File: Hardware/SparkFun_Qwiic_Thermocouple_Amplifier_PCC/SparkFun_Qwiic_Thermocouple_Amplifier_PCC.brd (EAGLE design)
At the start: 22.9 x 39.4 mm, 49 parts, among them J1 PTH, U16 MCP9600-SMD

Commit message: Added screw terminal board
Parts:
- removed I2C: (no value), SparkFun-Jumpers:SMT-JUMPER_3_2-NC_TRACE_SILK
- removed U16: MCP9600-SMD, MCP9600:MQFN-20
- added J5: PCB_THERMOCOUPLE, SparkFun-Electromechanical:PCC-SMP
- added U$15: (no value), buzzard_labels (7):ADR_#_0X660
- added U1: MCP9600-SMD, SparkFun-IC-Conversion:MQFN-20
- J1: device SparkX:1X04_NO_SILK -> SparkFun-Connectors:1X04_NO_SILK
- J2, J3: value (none) -> QWIIC
- JP2: value PCB_THERMOCOUPLE -> I2C; device MCP9600:PCC-SMP -> SparkFun-Jumpers:SMT-JUMPER_3_2-NC_TRACE_SILK
- moved JP2 8.71 mm to (15.9, 16.6), flipped to the top
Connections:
- net !ALT1: now also U1.11; no longer U16.11
- net !ALT2: now also U1.12; no longer U16.12
- net !ALT3: now also U1.14; no longer U16.14
- net !ALT4: now also U1.15; no longer U16.15
- net 3.3V: now also JP2.2, U1.8; no longer I2C.2, U16.8
- net ADDR: now also U1.16; no longer U16.16
- net GND: now also U1.1, U1.10, U1.13, U1.17, U1.18, U1.21, U1.3, U1.5, U1.6, U1.7, U1.9; no longer U16.1, U16.10, U16.13, U16.17, U16.18, U16.21, U16.3, U16.5, U16.6, U16.7, U16.9
- net N$2: now also JP2.1; no longer I2C.1
- net N$3: now also JP2.3; no longer I2C.3
- net N$4: now also J5.+, U1.2; no longer JP2.+, U16.2
- net N$5: now also J5.-, U1.4; no longer JP2.-, U16.4
- net SCL: now also U1.19; no longer U16.19
- net SDA: now also U1.20; no longer U16.20

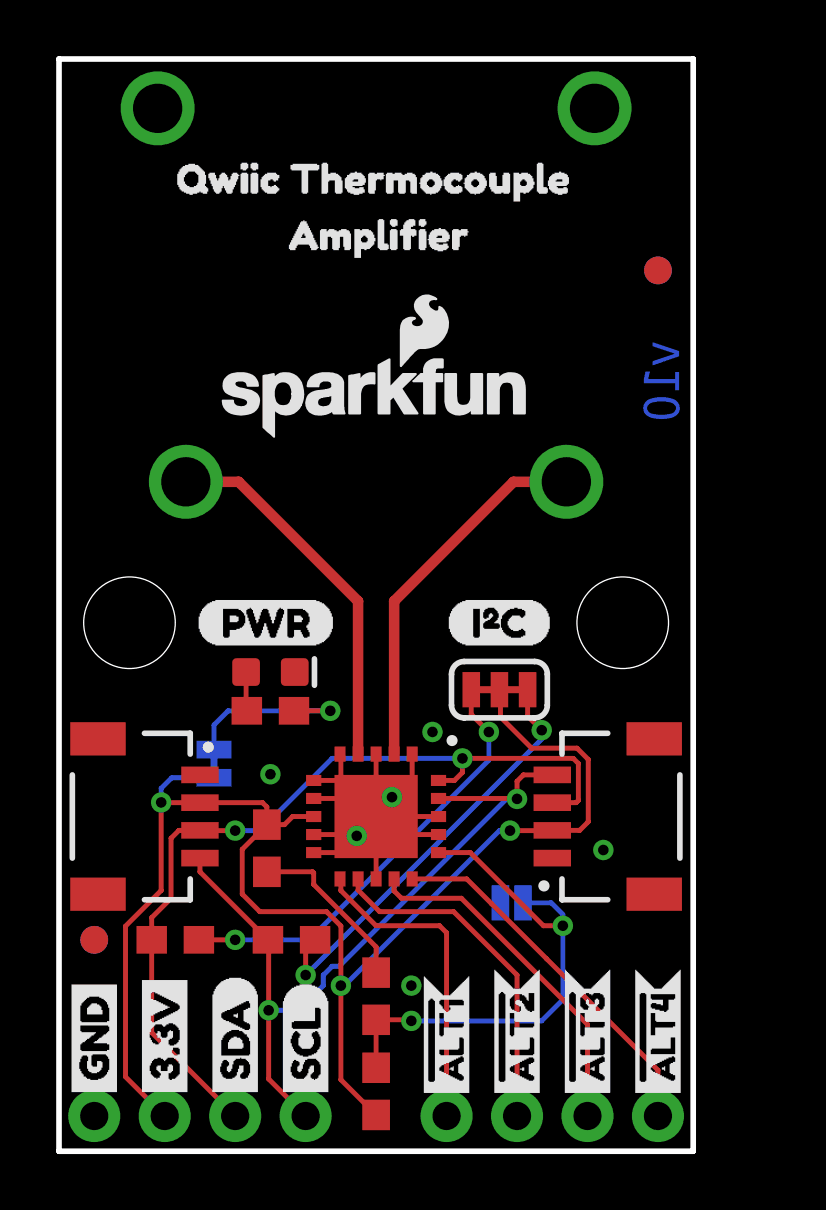
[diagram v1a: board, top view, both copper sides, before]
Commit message: Design review changes
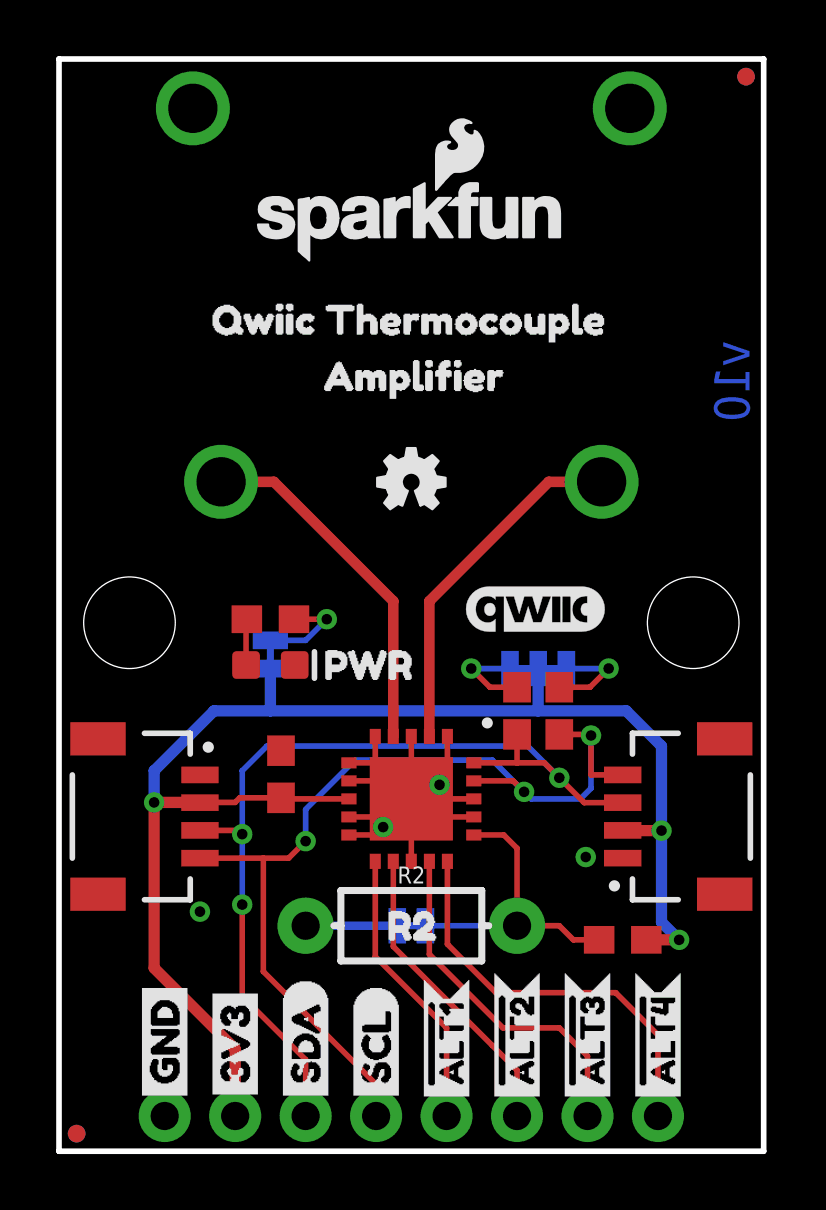
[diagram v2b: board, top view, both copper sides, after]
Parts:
- FD1, FD2, FD3, FD4: value FIDUCIAL1X2 -> FIDUCIALUFIDUCIAL; device SparkFun-Aesthetics:FIDUCIAL-1X2 -> SparkFun-Aesthetics:FIDUCIAL-MICRO
- JP1: device SparkFun-Jumpers:SMT-JUMPER_2_NO_SILK -> SparkFun-Jumpers:SMT-JUMPER_2_NC_TRACE_SILK
- LOGO2: value SFE_LOGO_NAME.1_INCH -> SFE_LOGO_NAME_FLAME.1_INCH; device SparkFun-Aesthetics:SFE_LOGO_NAME_.1 -> SparkFun-Aesthetics:SFE_LOGO_NAME_FLAME_.1
- R2: value 43k -> (none); device SparkFun-Resistors:0603 -> SparkFun-Resistors:AXIAL-0.3-KIT
- U$15: device buzzard_labels (7):ADR_#_0X660 -> buzzard_labels (8):PWR0
- U$16: device buzzard_labels (1):LED1 -> buzzard_labels:3V31
- U$19: device Labels:3.3V -> buzzard_labels:3V31
- U$2: device buzzard_labels (1):ADR_#_0X600 -> buzzard_labels (8):R21
- U$20: device Labels:PWR-()-04 -> buzzard_labels (6):LED0
- U$22: device Labels:3.3V -> buzzard_labels (9):ADDR1
- moved R4 14.8 mm to (16.5, 15.9), turned to 90 degrees
- moved U$22 14.4 mm to (15.6, 9.91), turned to 0 degrees
- moved R5 12.7 mm to (18.0, 15.9), turned to 90 degrees
- moved U$16 12.5 mm to (6.35, 1.52), turned to 90 degrees
- moved R3 10.4 mm to (20.3, 7.62), turned to 0 degrees
- moved U$15 9.71 mm to (8.64, 17.5), flipped to the top
- moved LOGO1 9.09 mm to (12.7, 24.1), flipped to the top
- moved U$20 7.83 mm to (12.7, 17.9), flipped to the bottom
- moved FD2 7.67 mm to (24.8, 38.7)
- moved FD3 7.67 mm to (24.8, 38.7)
- moved FD1 7.01 mm to (0.64, 0.64)
- moved FD4 7.01 mm to (0.64, 0.64)
- moved LOGO2 6.60 mm to (12.7, 12.4)
- moved U$17 6.48 mm to (12.7, 33.5)
- moved U$25 5.24 mm to (8.64, 27.9)
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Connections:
- net ADDR: now also R2.P$2; no longer R2.1
- net GND: now also R2.P$1; no longer R2.2
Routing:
- net N$3: track 15.9 -> 3.33 mm, vias 2 -> 1
- net N$2: track 15.4 -> 3.58 mm, vias 2 -> 1
- net ADDR: track 19.0 -> 11.0 mm, vias 2 -> 0
- net SCL: track 28.0 -> 35.6 mm, vias 2 -> 3
- net GND: track 26.4 -> 32.3 mm, vias 6 -> 4
- net N$6: track 6.60 -> 3.53 mm
- net SDA: track 31.3 -> 34.3 mm, vias 2 -> 3
- net !ALT4: track 13.4 -> 14.9 mm
- net !ALT2: track 12.5 -> 11.0 mm
- net !ALT1: track 11.5 -> 10.2 mm
- net N$5: track 13.5 -> 12.9 mm
- net N$4: track 13.5 -> 12.9 mm
- net 3.3V: track 54.0 -> 53.4 mm
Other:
- board size 22.9 x 39.4 mm -> 25.4 x 39.4 mm
